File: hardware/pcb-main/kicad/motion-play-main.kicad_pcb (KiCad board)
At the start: 4 copper layers, 86.4 x 35 mm, 37 parts, among them IC1 SN74AHCT125PWR, J2 DWEII Power Module, J3 LED_Strip, J4 Conn_01x05, J5 Conn_01x05, J6 Conn_01x05, U1 AP2112K-3.3TRG1, U2 T-Display-S3, U4 TCA9548APWR

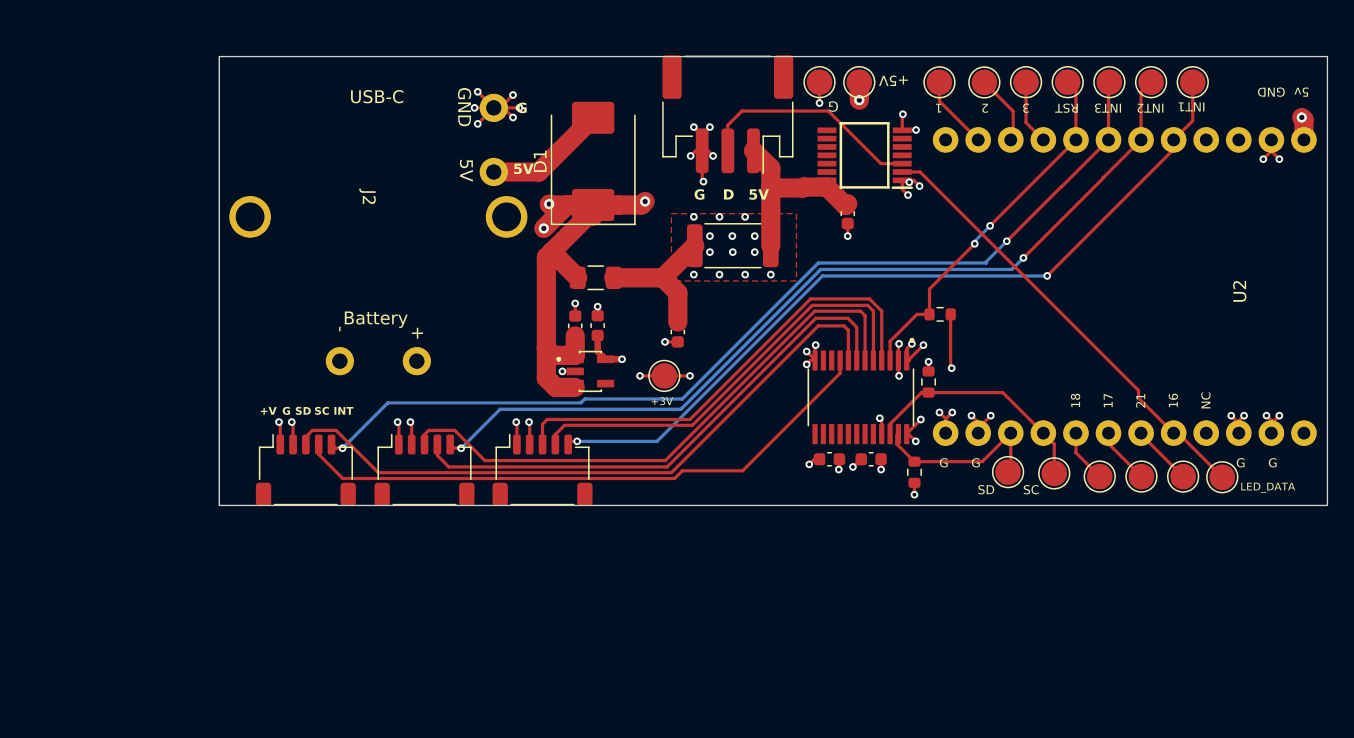
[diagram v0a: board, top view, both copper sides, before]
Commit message: Phase 3 validation: run placement pipeline, fix kiutils KiCad 9 writer, verify distances
- Run full extract→place pipeline: 46 components placed (0 failures, 4 relaxed)
- Fix place_power.py writer: replace kiutils Board.to_file (converts uuid→tstamp,
  breaks KiCad 9 format) with text-based regex replacement that preserves formatting
- Validate critical distances: L2 edge↔U6 SW 0.8mm, C32↔U6 BOOT 2.5mm,
  C34-C36↔U6 +5V 2.5-3.5mm. C23↔U5 BTST 4.5mm (relaxed, L1 blocks ideal spot)
- PCB updated with all 86 footprints (49 power components from schematic import)
- Update initiative docs: integrated-power and pcb-auto-placement TASKS/PLAN

Made-with: Cursor
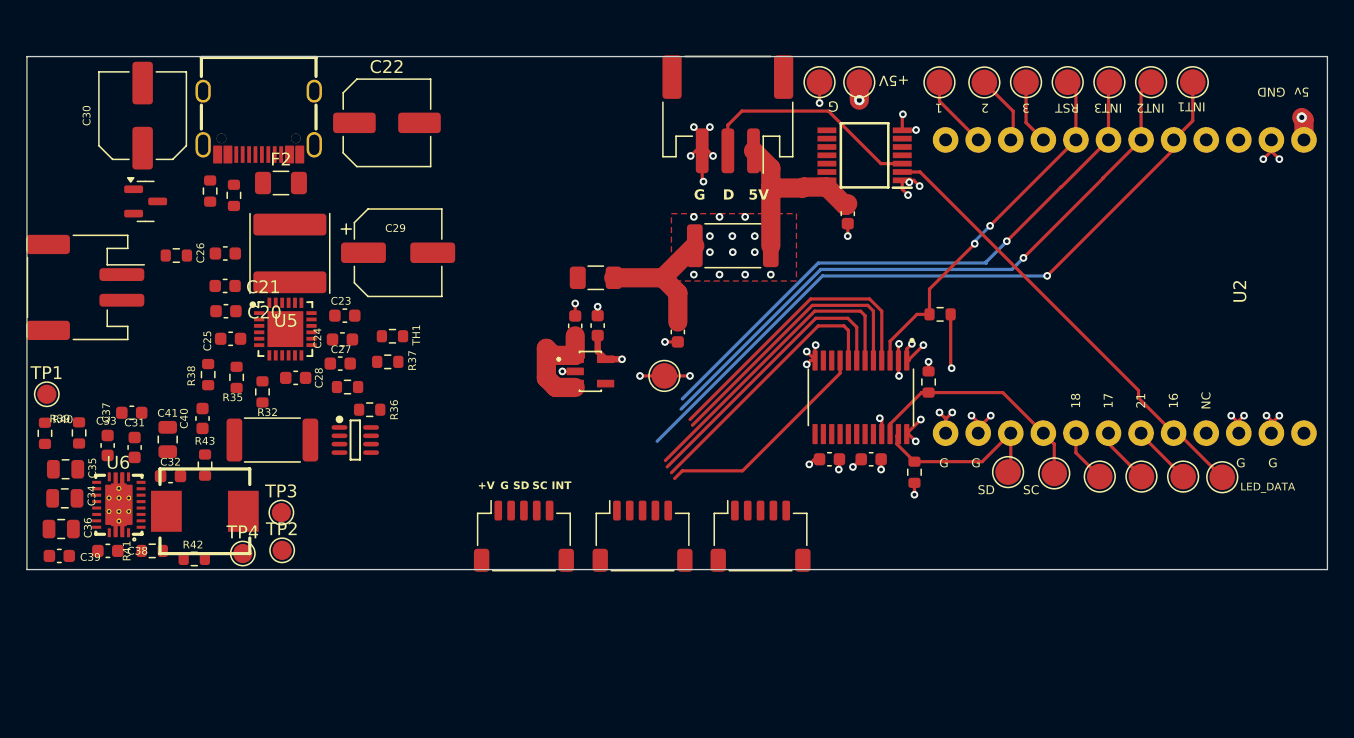
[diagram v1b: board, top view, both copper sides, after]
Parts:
- removed D1: D_Schottky, Diode_SMD:D_SMC
- removed J2: DWEII Power Module, motion-play-footprints:USBC_Power_Module
- added C20: 1µF, Capacitor_SMD:C_0603_1608Metric, F.Cu at (78.1, 120.9)
- added C21: 4.7µF, Capacitor_SMD:C_0603_1608Metric, F.Cu at (78.1, 118.9)
- added C22: 47µF 16V, Capacitor_SMD:C_Elec_6.3x5.4, F.Cu at (90.7, 106.2)
- added C23: 47nF, Capacitor_SMD:C_0603_1608Metric, F.Cu at (87.4, 121.2)
- added C24: 4.7µF, Capacitor_SMD:C_0603_1608Metric, F.Cu at (87.2, 123.1)
- added C25: 10µF, Capacitor_SMD:C_0603_1608Metric, F.Cu at (78.5, 123.0)
- added C26: 10µF, Capacitor_SMD:C_0603_1608Metric, F.Cu at (78.1, 116.4)
- added C27: 10µF, Capacitor_SMD:C_0603_1608Metric, F.Cu at (87.0, 124.9)
- added C28: 10µF, Capacitor_SMD:C_0603_1608Metric, F.Cu at (83.6, 126.1)
- added C29: 220µF 10V, Capacitor_SMD:CP_Elec_6.3x7.7, F.Cu at (91.5, 116.3)
- added C30: 47µF 10V, Capacitor_SMD:C_Elec_6.3x5.4, F.Cu at (71.6, 105.6)
- added C31: 0.1µF, Capacitor_SMD:C_0603_1608Metric, F.Cu at (71.0, 131.5)
- added C32: 0.1µF, Capacitor_SMD:C_0603_1608Metric, F.Cu at (73.8, 133.7)
- added C33: 2.2µF, Capacitor_SMD:C_0603_1608Metric, F.Cu at (68.9, 131.3)
- added C34: 22µF, Capacitor_SMD:C_0805_2012Metric, F.Cu at (65.6, 135.4)
- added C35: 22µF, Capacitor_SMD:C_0805_2012Metric, F.Cu at (65.6, 133.2)
- added C36: 22µF, Capacitor_SMD:C_0805_2012Metric, F.Cu at (65.3, 137.8)
- added C37: 47nF, Capacitor_SMD:C_0603_1608Metric, F.Cu at (70.8, 128.8)
- added C38: 4.7nF, Capacitor_SMD:C_0603_1608Metric, F.Cu at (68.9, 139.5)
- added C39: 100pF, Capacitor_SMD:C_0603_1608Metric, F.Cu at (65.1, 139.9)
- added C40: 0.1µF, Capacitor_SMD:C_0603_1608Metric, F.Cu at (76.3, 129.2)
- added C41: 10µF, Capacitor_SMD:C_0805_2012Metric, F.Cu at (73.6, 130.9)
- added F2: 3A, Fuse:Fuse_1206_3216Metric, F.Cu at (82.4, 110.9)
- added J7: TYPE-C-31-M-12, TYPE-C-31-M-12:USB-C_SMD-TYPE-C-31-M-12_1, F.Cu at (80.7, 106.2)
- added J8: JST_PH_2pin, Connector_JST:JST_PH_S2B-PH-SM4-TB_1x02-1MP_P2.00mm_Horizontal, F.Cu at (67.2, 119.0)
- added L1: 2.2µH, Inductor_SMD:L_Changjiang_FNR6028S, F.Cu at (83.1, 116.3)
- added L2: 2.2µH 10A, FXL0630-2R2-M:IND-SMD_L7.0-W6.6, F.Cu at (76.5, 136.5)
- added Q2: PMOS, Package_TO_SOT_SMD:SOT-23, F.Cu at (71.9, 112.3)
- added R30: 5.1kΩ, Resistor_SMD:R_0603_1608Metric, F.Cu at (78.7, 111.8)
- added R31: 5.1kΩ, Resistor_SMD:R_0603_1608Metric, F.Cu at (76.9, 111.5)
- added R32: 330Ω, Resistor_SMD:R_0603_1608Metric, F.Cu at (81.0, 127.1)
- added R33: 100kΩ, Resistor_SMD:R_0603_1608Metric, F.Cu at (87.6, 126.8)
- added R34: 100kΩ, Resistor_SMD:R_0603_1608Metric, F.Cu at (74.2, 116.5)
- added R35: 10kΩ, Resistor_SMD:R_0603_1608Metric, F.Cu at (78.9, 126.0)
- added R36: 5.6kΩ, Resistor_SMD:R_0603_1608Metric, F.Cu at (89.3, 128.5)
- added R37: 30kΩ, Resistor_SMD:R_0603_1608Metric, F.Cu at (90.7, 124.8)
- added R38: 10kΩ, Resistor_SMD:R_0603_1608Metric, F.Cu at (76.7, 125.8)
- added R39: 180kΩ, Resistor_SMD:R_0603_1608Metric, F.Cu at (66.7, 130.3)
- added R40: 56kΩ, Resistor_SMD:R_0603_1608Metric, F.Cu at (64.0, 130.4)
- added R41: 100kΩ, Resistor_SMD:R_0603_1608Metric, F.Cu at (72.4, 139.5)
- added R42: 100kΩ, Resistor_SMD:R_0603_1608Metric, F.Cu at (75.6, 140.2)
- added R43: 22kΩ, Resistor_SMD:R_0603_1608Metric, F.Cu at (76.5, 132.9)
- added R44: 10mΩ, Resistor_SMD:R_2512_6332Metric, F.Cu at (81.7, 130.9)
- added TH1: 10kΩ NTC, Resistor_SMD:R_0603_1608Metric, F.Cu at (91.1, 122.8)
- added TP1: VSYS, TestPoint:TestPoint_Pad_D1.5mm, F.Cu at (64.1, 127.3)
- added TP2: VBAT, TestPoint:TestPoint_Pad_D1.5mm, F.Cu at (82.5, 139.5)
- added TP3: PVBUS, TestPoint:TestPoint_Pad_D1.5mm, F.Cu at (82.4, 136.6)
- added TP4: PGND, TestPoint:TestPoint_Pad_D1.5mm, F.Cu at (79.4, 139.8)
- added U5: BQ24195RGER, BQ24195RGET:VQFN-24_L4.0-W4.0-P0.50-TL-EP2.8, F.Cu at (82.8, 122.2)
- added U6: TPS61088RHLR, TPS61088RHLR:VQFN-20_L4.6-W3.6-P0.50-BL, F.Cu at (69.8, 135.9)
- added U7: INA219AIDCNR, INA219AIDCNR:SOT-23-8_L3.0-W1.7-P0.65-LS2.8-BR, F.Cu at (88.2, 130.9)
- moved J4 17.8 mm to (119.8, 138.4)
- moved J5 17.8 mm to (110.6, 138.4)
- moved J6 17.8 mm to (101.3, 138.4)
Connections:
- net Net-(U2-21) renamed /Power Management/CHRG_INT
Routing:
- net /TCA9548A_Subsystem/CH2_SDA: track 51.7 -> 21.0 mm
- net /TCA9548A_Subsystem/CH2_SCL: track 46.6 -> 17.3 mm
- net /INT3: track 75.7 -> 46.6 mm, vias 2 -> 1
- net +5V: track 42.3 -> 14.1 mm, vias 5 -> 2
- net /TCA9548A_Subsystem/CH1_SDA: track 44.7 -> 24.0 mm
- net /INT2: track 69.0 -> 49.6 mm, vias 2 -> 1
- net /TCA9548A_Subsystem/CH1_SCL: track 41.6 -> 22.5 mm
- net GND: track 66.3 -> 50.1 mm, vias 58 -> 49
- net /TCA9548A_Subsystem/CH0_SDA: track 36.3 -> 23.1 mm
- net /TCA9548A_Subsystem/CH0_SCL: track 33.8 -> 22.0 mm
- net Net-(D1-A): track 9.50 -> 0.00 mm
- net /INT1: track 62.6 -> 55.6 mm, vias 2 -> 1
- net +3.3V: track 22.7 -> 17.3 mm, vias 13 -> 10
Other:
- board size 86.4 x 35 mm -> 101.4 x 40 mm
